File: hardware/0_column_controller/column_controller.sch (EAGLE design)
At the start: 45 parts, among them J4 JTAG, U1 ESP-WROVER-32ESP-WROVER-32, U2 3.3V, U3 CP2102N

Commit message: increase standoff size column controller
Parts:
- H1, H2, H3, H4: value STAND-OFF -> STAND-OFF#8; device SparkFun-Hardware:STAND-OFF -> standoff:STAND-OFF#8
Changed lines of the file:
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@@
 <part name="SUPPLY12" library="SparkFun-PowerSymbols" deviceset="VIN" device=""/>
 <part name="GND12" library="SparkFun-PowerSymbols" deviceset="GND" device=""/>
-<part name="H1" library="SparkFun-Hardware" deviceset="STAND-OFF" device=""/>
-<part name="H2" library="SparkFun-Hardware" deviceset="STAND-OFF" device=""/>
-<part name="H3" library="SparkFun-Hardware" deviceset="STAND-OFF" device=""/>
-<part name="H4" library="SparkFun-Hardware" deviceset="STAND-OFF" device=""/>
+<part name="H1" library="standoff" deviceset="STAND-OFF" device="#8"/>
+<part name="H2" library="standoff" deviceset="STAND-OFF" device="#8"/>
+<part name="H3" library="standoff" deviceset="STAND-OFF" device="#8"/>
+<part name="H4" library="standoff" deviceset="STAND-OFF" device="#8"/>
 <part name="FD1" library="SparkFun-Aesthetics" deviceset="FIDUCIAL" device="1X2"/>
 <part name="FD2" library="SparkFun-Aesthetics" deviceset="FIDUCIAL" device="1X2"/>

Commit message: prepare for v10 generation
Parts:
- J1: device SparkFun-Connectors:CONN_02SCREWTERMINAL-6.35MM-2 -> SparkFun-Connectors:CONN_04SCREW_LOCK
- R2, R3: value 2.2k -> 1k; device SparkFun-Resistors:2.2KOHM-0603-1/10W-1% -> SparkFun-Resistors:1KOHM-0603-1/10W-1%
- R4, R9: value 33 -> 330; device SparkFun-Resistors:33OHM-0603-1/10W-1% -> SparkFun-Resistors:330OHM-0603-1/10W-1%
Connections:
- net GND: now also J1.3, J1.4; no longer J1.1
- net VIN: now also J1.1
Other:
- moved on the sheet: J2

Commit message: update controller board
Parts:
- removed FRAME1: FRAME-LEDGER, SparkFun-Aesthetics:FRAME-LEDGER
- removed J2: (no value), SparkFun-Connectors:CONN_021X02_NO_SILK
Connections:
- net GND: no longer J2.1
- net VIN: no longer J2.2

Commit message: add frame and organize
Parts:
- added FRAME1: FRAME-LETTER, SparkFun-Aesthetics:FRAME-LETTER
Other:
- moved on the sheet: C1, C10, C11, C2, C3, C4, C5, C6, C7, C8, C9, D1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

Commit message: begin change to differential I2C solution
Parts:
- removed C5: 4.7uF, SparkFun-Capacitors:4.7UF-0603-35V-(20%)
- removed FD1, FD2, FD3, FD4: FIDUCIAL1X2, SparkFun-Aesthetics:FIDUCIAL1X2
- removed Q1: (no value), SparkFun-DiscreteSemi:TRANS_NPN_DUAL-MBT3904DW1T1
- removed U2: 3.3V, SparkFun-IC-Power:V_REG_AP2112K-3.3V
- removed U3: CP2102N, SparkFun-IC-Comms:CP2102N
- added D11: RED, SparkFun-LED:LED-RED0603
- added J7: RJ45, SparkFun-Connectors:RJ45-8
- added JP1, PWR: JUMPER-SMT_2_NC_TRACE_SILK, SparkFun-Jumpers:JUMPER-SMT_2_NC_TRACE_SILK
- added JP2, JP3: JUMPER-SMT_3_2-NC_TRACE_SILK, SparkFun-Jumpers:JUMPER-SMT_3_2-NC_TRACE_SILK
- added JP4: JUMPER-SMT_2_NO_SILK, SparkFun-Jumpers:JUMPER-SMT_2_NO_SILK
- added R12: 1k, SparkFun-Resistors:1KOHM-0603-1/10W-1%
- added U$13: SAMD21_MINI_BREAKOUT, SparkFun-Boards:SAMD21_MINI_BREAKOUT
- C3, C4: device SparkFun-Capacitors:1.0UF-0603-16V-10%-X7R -> SparkFun-Capacitors:1.0UF-0603-16V-10%
- D1: value 13 -> BLUE
- D2, D3: value 3A/10V/280mV -> BLUE; device SparkFun-DiscreteSemi:DIODE-SCHOTTKY-BAT60A -> SparkFun-LED:LED-BLUE0603
- D4: value POWER -> BLUE; device SparkFun-LED:LED-RED0603 -> SparkFun-LED:LED-BLUE0603
- J3: value (none) -> RJ45; device SparkFun-Connectors:USB_C_2-LAYER -> SparkFun-Connectors:RJ45-8
- R1, R6: value 10k -> 1k; device SparkFun-Resistors:10KOHM-0603-1/10W-1% -> SparkFun-Resistors:1KOHM-0603-1/10W-1%
- R10, R11: value 5.1k -> 1k; device SparkFun-Resistors:5.1KOHM5.1KOHM-0603-1/10W-1% -> SparkFun-Resistors:1KOHM-0603-1/10W-1%
- R4, R9: value 330 -> 1k; device SparkFun-Resistors:330OHM-0603-1/10W-1% -> SparkFun-Resistors:1KOHM-0603-1/10W-1%
- R5: value 10k -> DNP; device SparkFun-Resistors:10KOHM-0603-1/10W-1% -> SparkFun-Resistors:RESISTOR0603
- R7: value 10 -> 1k; device SparkFun-Resistors:10OHM-0603-1/10W-1% -> SparkFun-Resistors:1KOHM-0603-1/10W-1%
- S1: value Button 0 -> MOMENTARY-SWITCH-SPST-SMD-5.2MM-TALL; device SparkFun-Switches:MOMENTARY-SWITCH-SPST-SMD-4.6X2.8MM -> SparkFun-Switches:MOMENTARY-SWITCH-SPST-SMD-5.2MM-TALL
- S2: value !RESET -> MOMENTARY-SWITCH-SPST-SMD-5.2MM-TALL; device SparkFun-Switches:MOMENTARY-SWITCH-SPST-SMD-4.6X2.8MM -> SparkFun-Switches:MOMENTARY-SWITCH-SPST-SMD-5.2MM-TALL
- U1: value ESP-WROVER-32ESP-WROVER-32 -> PCA9615; device SparkFun-RF:ESP-WROVER-32ESP-WROVER-32 -> SparkFun-IC-Comms:PCA9615
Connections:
- removed net !RESET: Q1Q1.C, R1.1, S2.2, U1.EN
- removed net 0: Q1Q2.C, S1.2, U1.IO0
- removed net 13: R4.2, U1.MOSI_H/IO13
- removed net DTR: Q1Q2.E, R5.2, U3.DTR
- removed net N$11: J3.CC2, R10.2
- removed net RTS: Q1Q1.E, R6.2, U3.RTS
- removed net RX: U1.TXD, U3.RXD
- removed net SCL: J4.!RESET, R2.1, U1.IO22
- removed net SDA: J4.NC/TDI, R3.1, U1.MOSI_V/IO23
- removed net SHLD: J3.SHLD
- removed net TX: U1.RXD, U3.TXD
- removed net VIN: D3.A, J1.1, J1.2
- removed net V_USB: D2.A, J3.VBUS, R7.1
- new net B0: R10.2, S1.1, U$13.PA18
- new net B1: R12.2, S2.1, U$13.PA19
- new net DSCL_N: J3.1, J7.1, U1.DSCL-
- new net DSCL_P: J3.2, J7.2, U1.DSCL+
- new net DSDA_N: J3.7, J7.7, U1.DSDA-
- new net DSDA_P: J3.8, J7.8, U1.DSDA+
- new net LED0: R6.1, U$13.PA10
- new net LED1: R7.1, U$13.PA11
- new net LED2: R8.1, U$13.PA14
- new net LED3: R9.1, U$13.PA15
- new net N$13: D11.C, R11.1
- new net N$14: PWR.2, R11.2
- new net N$9: D2.A, R7.2
- new net PCA_EN: JP4.2, U1.EN
- new net SCL_COLUMN: J4.!RESET, R2.1, U$13.PA09
- new net SCL_NETWORK: R1.1, U$13.PA17, U1.SCL
- new net SDA_COLUMN: J4.NC/TDI, R3.1, U$13.PA08
- new net SDA_NETWORK: R4.1, U$13.PA16, U1.SDA
- net 3.3V: now also C1.1, C3.1, D11.A, JP2.2, JP3.2, R10.1, R12.1, U$13.3V3, U1.VDDA, U1.VDDB; no longer C5.1, R1.2, R2.2, R3.2, R8.2, R9.2, U1.3V3, U2.OUT, U3.VDD, U3.VIO
- net 5V: now also J1.3, J1.4, J3.3, J7.3, U$13.AREF, U$13.VIN; no longer C1.1, C3.1, D2.C, D3.C, U2.EN, U2.IN
- net DOUT: now also JP1.2, R5.2; no longer U1.SCK_V/IO18
- net GND: now also D2.C, D3.C, J1.1, J1.2, J3.6, J7.6, PWR.1, S1.2, S2.2, U$13.GND; no longer C5.2, J1.3, J1.4, J3.GND, R10.1, R11.1, S1.1, S2.1, U1.GND@1, U1.GND@15, U1.GND@38, U2.GND, U3.GND
- net N$1: now also JP1.1, R5.1, U$13.PA20; no longer J3.D-, U3.D-
- net N$10: now also JP4.1, U$13.PB09; no longer J3.CC1, R11.2
- net N$2: now also JP2.3, R1.2; no longer J3.D+, U3.D+
- net N$3: now also JP2.1, R4.2; no longer Q1Q2.B, R6.1
- net N$4: now also JP3.3, R2.2; no longer D1.A, R4.1
- net N$5: now also JP3.1, R3.2; no longer Q1Q1.B, R5.1
- net N$6: now also D1.A, R6.2; no longer R7.2, U3.VBUS, U3.VREGIN
- net N$7: now also D4.A, R9.2; no longer R8.1, U3.!RSTB
- net N$8: now also D3.A, R8.2; no longer D4.A, R9.1
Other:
- note added: "Cut the PWR jumper to disable the PWR LED"
- moved on the sheet: C1, C10, C11, C2, C3, C4, C6, C7, C8, C9, D1, D4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

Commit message: proto schematic for v11 column controller
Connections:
- new net RXI: U$13.PA11
- new net TXO: U$13.PA10
- net 5V: now also J3.4, J7.4
- net GND: now also J3.5, J7.5
- net LED0: now also U$13.PA02; no longer U$13.PA10
- net LED1: now also U$13.PA04; no longer U$13.PA11
- net LED2: now also U$13.PA06; no longer U$13.PA14
- net LED3: now also U$13.PA07; no longer U$13.PA15
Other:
- note added: "16 nodes + 1 controller chained using the RJ45 diff i2c connection"
- note added: "Headers"
- note added: "PCA 9615"
- note added: "Passives"
- note added: "User I/O"
- note added: "bulk caps for 5V line out to column meant to supply LED switching current"
- note added: "can inject 5V to system on this power header"
- note added: "col i2c on sercom 0"
- note added: "column i2c samples 3.3v sensors on the column"
- note added: "network i2c communicates between the SAMD21s over differential transport"
- note added: "network i2c on sercom 1"
- note added: "relying on SAMD21 mini breakout voltage regulator for 5V to 3.3V conversion"
- note added: "uart on sercom 2"
- note added: "using grn/wht + blu/wht pairs for power w/ least voltage drop"
- moved on the sheet: JP1, JP4, R5

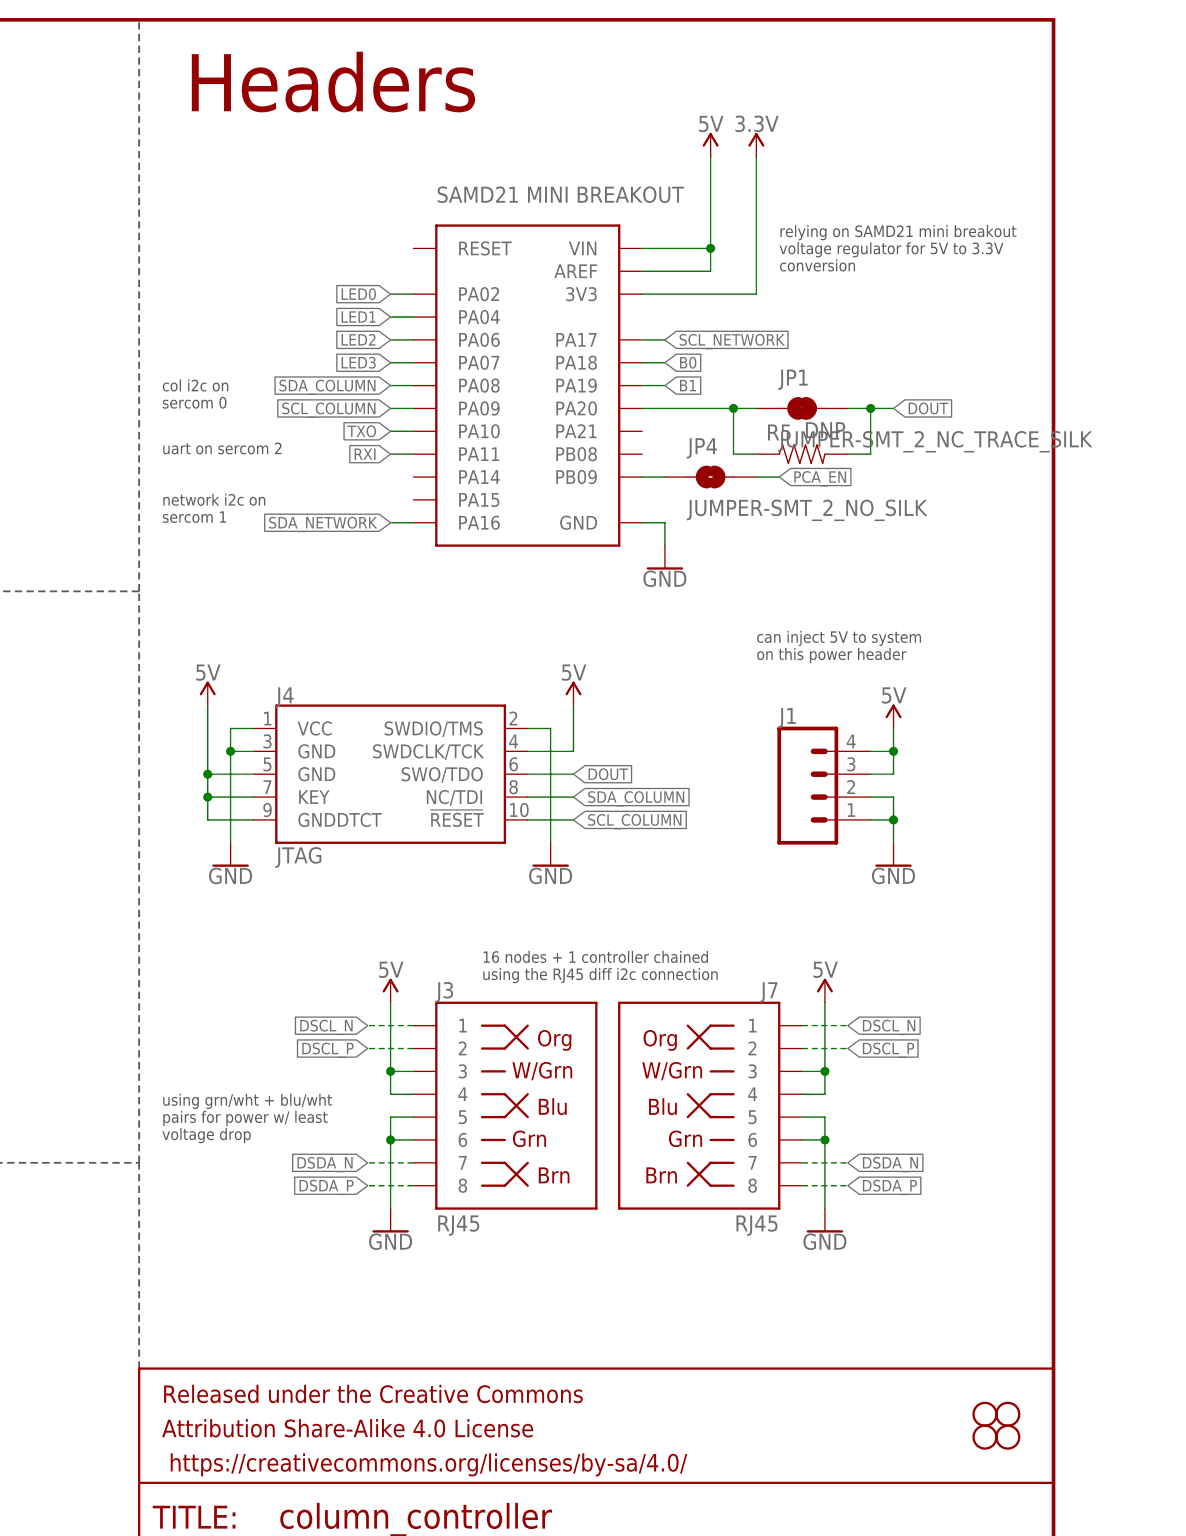
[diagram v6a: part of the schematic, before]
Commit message: add uart / i2c / column debug access headers
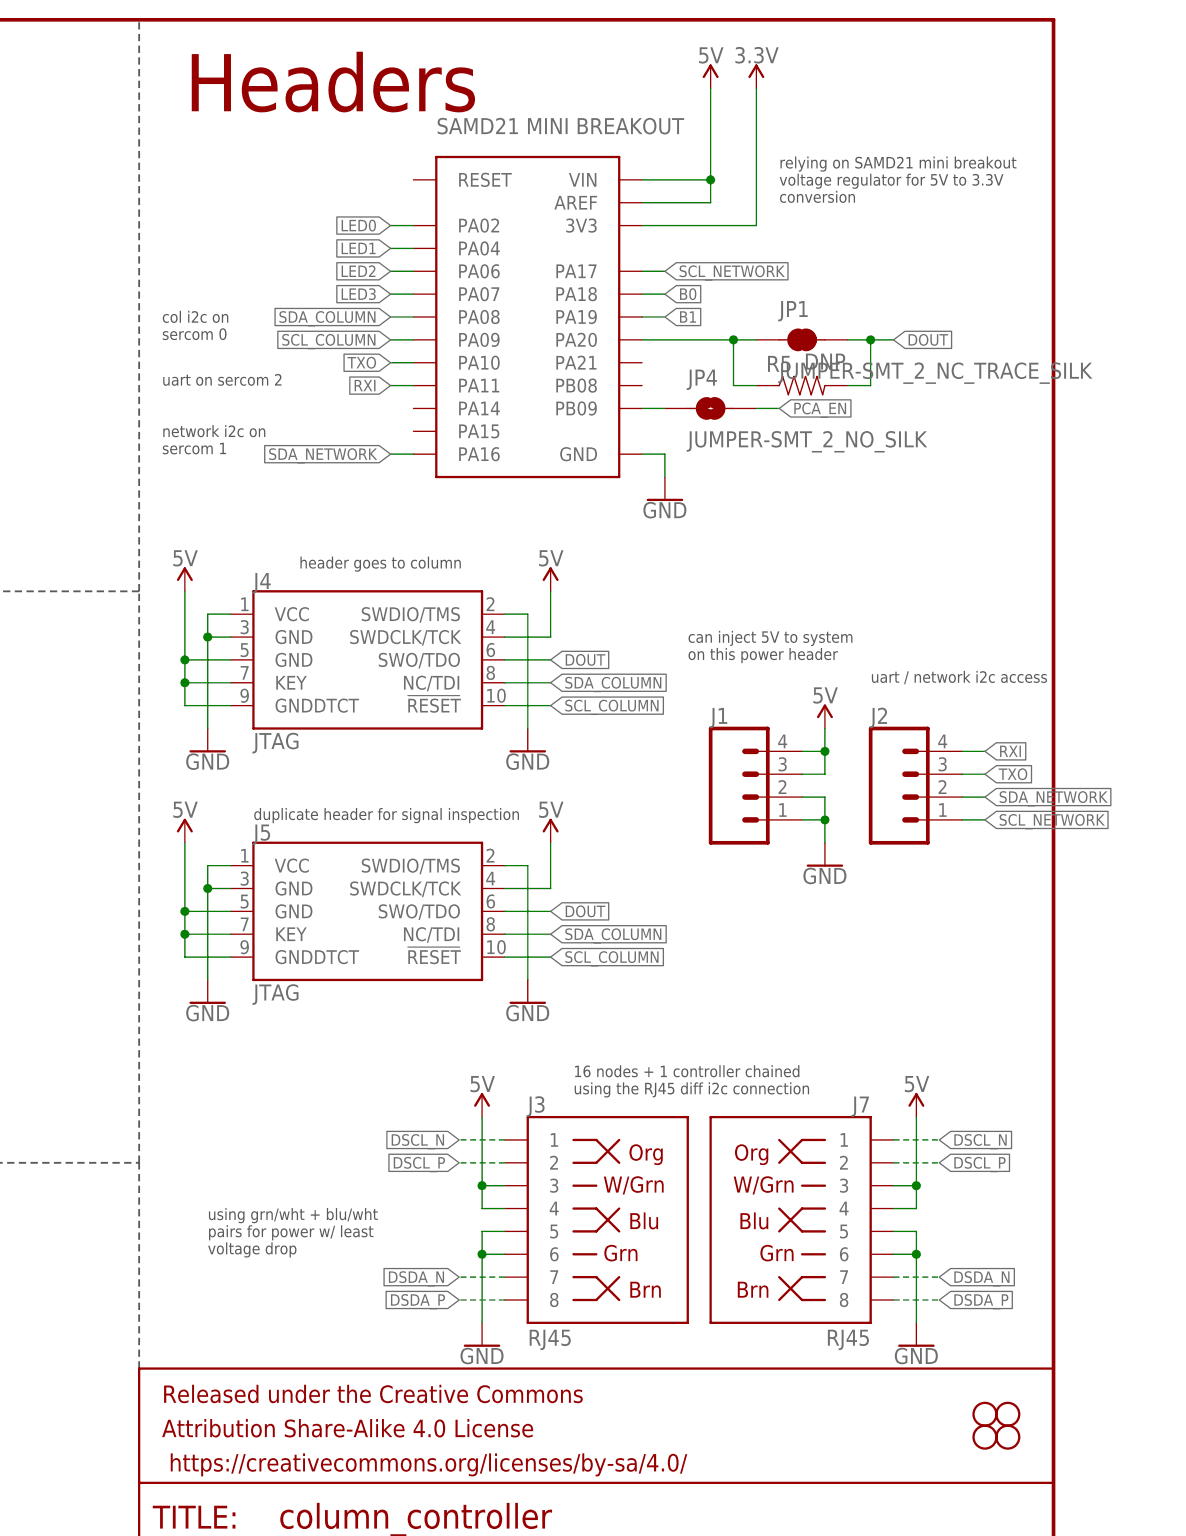
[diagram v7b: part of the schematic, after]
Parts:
- added J2: (no value), SparkFun-Connectors:CONN_04SCREW_LOCK
- added J5: JTAG, SparkFun-Connectors:CORTEX_JTAG_DEBUG_SMD
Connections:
- net 5V: now also J5.GND@5, J5.GNDDTCT, J5.KEY, J5.SWDCLK/TCK
- net DOUT: now also J5.SWO/TDO
- net GND: now also J5.GND@3, J5.SWDIO/TMS, J5.VCC
- net RXI: now also J2.4
- net SCL_COLUMN: now also J5.!RESET
- net SCL_NETWORK: now also J2.1
- net SDA_COLUMN: now also J5.NC/TDI
- net SDA_NETWORK: now also J2.2
- net TXO: now also J2.3
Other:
- note added: "duplicate header for signal inspection"
- note added: "header goes to column"
- note added: "uart / network i2c access"
- moved on the sheet: J1, J3, J4, J7, JP1, JP4, R5

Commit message: redesign + order column_controller board
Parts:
- removed D11: RED, SparkFun-LED:LED-RED0603
- removed PWR: JUMPER-SMT_2_NC_TRACE_SILK, SparkFun-Jumpers:JUMPER-SMT_2_NC_TRACE_SILK
- removed R11: 1k, SparkFun-Resistors:1KOHM-0603-1/10W-1%
- added J6, J8, J9: (no value), SparkFun-Connectors:CONN_031X03_NO_SILK
- C3, C4: device SparkFun-Capacitors:1.0UF-0603-16V-10% -> SparkFun-Capacitors:1.0UF-0603-16V-10%-X7R
- J2: device SparkFun-Connectors:CONN_04SCREW_LOCK -> SparkFun-Connectors:CONN_031X03_NO_SILK
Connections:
- removed net N$13: D11.C, R11.1
- removed net N$14: PWR.2, R11.2
- net 3.3V: no longer C2.1, C4.1, D11.A, U1.VDDB
- net 5V: now also C2.1, C4.1, U1.VDDB
- net GND: now also J2.1, J6.1, J8.1, J9.1; no longer PWR.1
- net RXI: now also J2.2, J8.2; no longer J2.4
- net SCL_NETWORK: now also J6.2, J9.2; no longer J2.1
- net SDA_NETWORK: now also J6.3, J9.3; no longer J2.2
- net TXO: now also J8.3
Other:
- note removed: "Cut the PWR jumper to disable the PWR LED"
